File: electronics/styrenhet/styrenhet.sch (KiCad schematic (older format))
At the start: 50 parts, among them J1 12V Fan, J2 Battery_In, J3 Battery to MCU, J4 12V Fan, J5 IDE PATA Connector, J6 Motor1_In, J7 Motor2_In, J8 Motor3_In, J9 Motor4_In, U1 motor_driver, U2 motor_driver, U3 motor_driver, U4 motor_driver

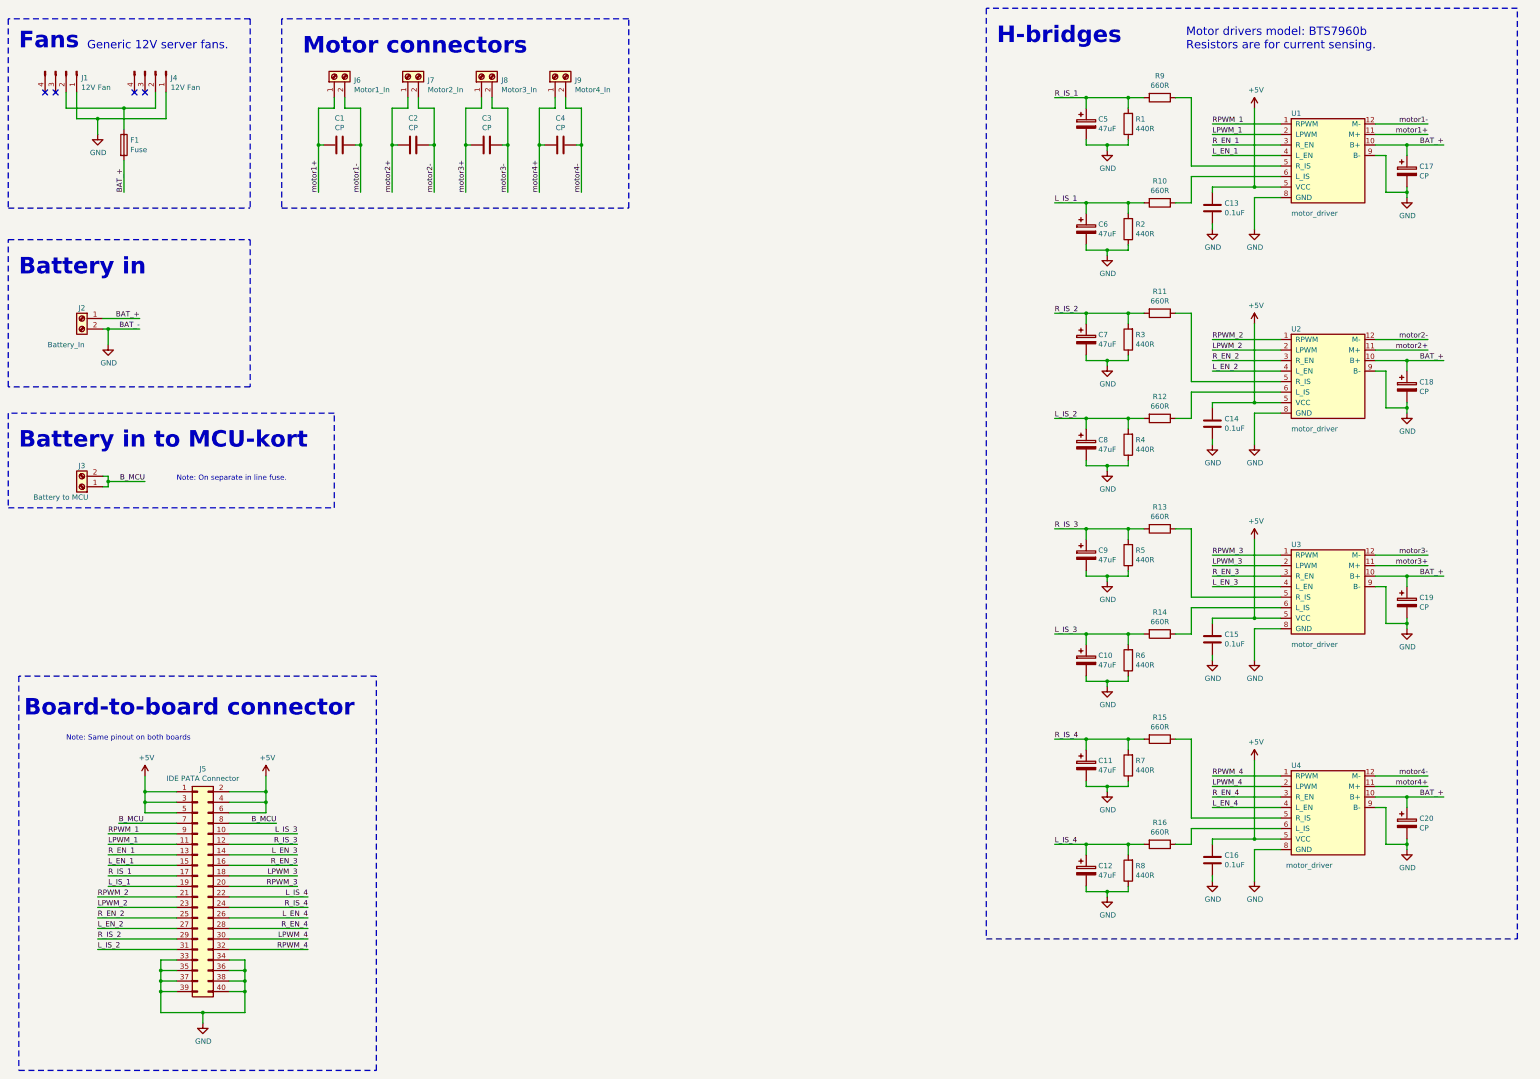
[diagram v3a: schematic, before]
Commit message: Placera h-bryggor.
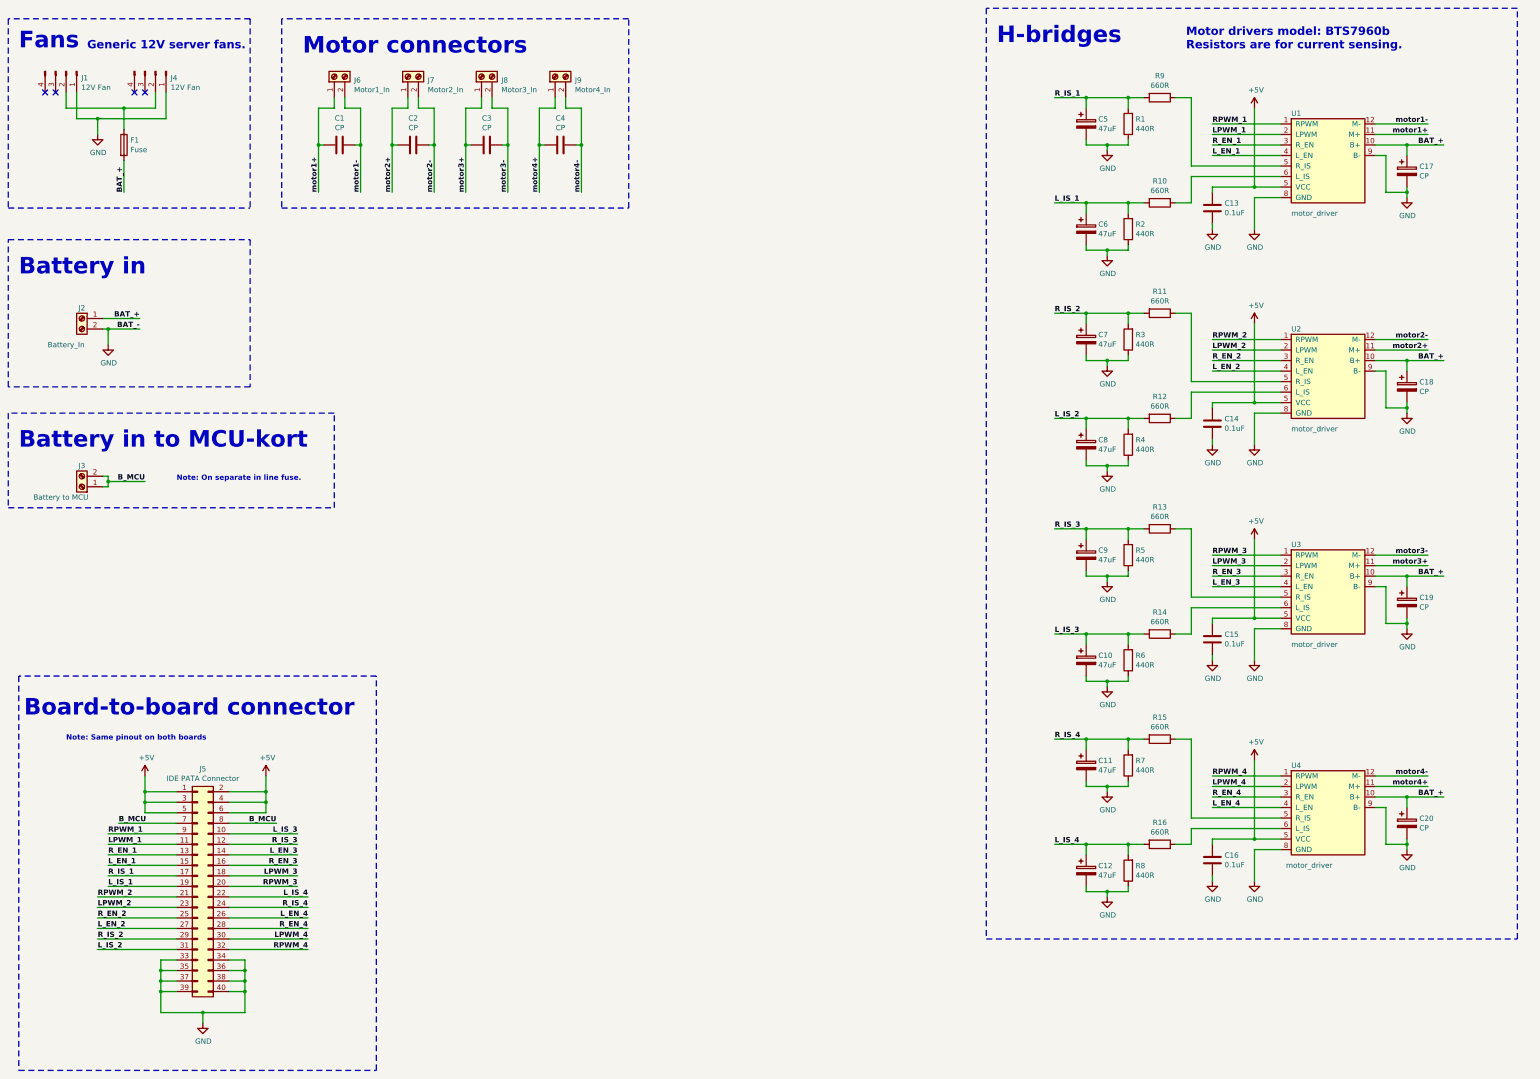
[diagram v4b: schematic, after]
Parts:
- U2, U3, U4: footprint styrenhet:motor-driver -> styrenhet-footprints:motor-driver
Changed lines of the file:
@@
 Wire Wire Line
 	12600 2750 12600 2800
-Text Label 12600 1800 0    50   ~ 0
+Text Label 12600 1800 0    50   ~ 6
 RPWM_1
 Wire Wire Line
 	12600 1800 13250 1800
-Text Label 12600 1900 0    50   ~ 0
+Text Label 12600 1900 0    50   ~ 6
 LPWM_1
 Wire Wire Line
 	12600 1900 13250 1900
-Text Label 12600 2000 0    50   ~ 0
+Text Label 12600 2000 0    50   ~ 6
 R_EN_1
-Text Label 12600 2100 0    50   ~ 0
+Text Label 12600 2100 0    50   ~ 6
 L_EN_1
-Text Label 11100 1550 0    50   ~ 0
+Text Label 11100 1550 0    50   ~ 6
 R_IS_1
 Wire Wire Line
@@
 F 0 "U2" H 13350 4650 50  0000 L CNN
 F 1 "motor_driver" H 13350 3700 50  0000 L CNN
-F 2 "styrenhet:motor-driver" H 13350 4150 50  0001 C CNN
+F 2 "styrenhet-footprints:motor-driver" H 13350 4150 50  0001 C CNN
 F 3 "" H 13350 4150 50  0001 C CNN
 	1    13700 4200
@@
 Wire Wire Line
 	12600 4800 12600 4850
-Text Label 12600 3850 0    50   ~ 0
+Text Label 12600 3850 0    50   ~ 6
 RPWM_2
 Wire Wire Line
 	12600 3850 13250 3850
-Text Label 12600 3950 0    50   ~ 0
+Text Label 12600 3950 0    50   ~ 6
 LPWM_2
 Wire Wire Line
 	12600 3950 13250 3950
-Text Label 12600 4050 0    50   ~ 0
+Text Label 12600 4050 0    50   ~ 6
 R_EN_2
-Text Label 12600 4150 0    50   ~ 0
+Text Label 12600 4150 0    50   ~ 6
 L_EN_2
-Text Label 11100 3600 0    50   ~ 0
+Text Label 11100 3600 0    50   ~ 6
 R_IS_2
-Text Label 11100 4600 0    50   ~ 0
+Text Label 11100 4600 0    50   ~ 6
 L_IS_2
 Wire Wire Line
@@
 Wire Wire Line
 	12600 6850 12600 6900
-Text Label 12600 5900 0    50   ~ 0
+Text Label 12600 5900 0    50   ~ 6
 RPWM_3
 Wire Wire Line
 	12600 5900 13250 5900
-Text Label 12600 6000 0    50   ~ 0
+Text Label 12600 6000 0    50   ~ 6
 LPWM_3
 Wire Wire Line
 	12600 6000 13250 6000
-Text Label 12600 6100 0    50   ~ 0
+Text Label 12600 6100 0    50   ~ 6
 R_EN_3
-Text Label 12600 6200 0    50   ~ 0
+Text Label 12600 6200 0    50   ~ 6
 L_EN_3
-Text Label 11100 5650 0    50   ~ 0
+Text Label 11100 5650 0    50   ~ 6
 R_IS_3
-Text Label 11100 6650 0    50   ~ 0
+Text Label 11100 6650 0    50   ~ 6
 L_IS_3
 Wire Wire Line
@@
 F 0 "U4" H 13350 8800 50  0000 L CNN
 F 1 "motor_driver" H 13300 7850 50  0000 L CNN
-F 2 "styrenhet:motor-driver" H 13350 8300 50  0001 C CNN
+F 2 "styrenhet-footprints:motor-driver" H 13350 8300 50  0001 C CNN
 F 3 "" H 13350 8300 50  0001 C CNN
 	1    13700 8350
@@
 Wire Wire Line
 	12600 8950 12600 9000
-Text Label 12600 8000 0    50   ~ 0
+Text Label 12600 8000 0    50   ~ 6
 RPWM_4
 Wire Wire Line
 	12600 8000 13250 8000
-Text Label 12600 8100 0    50   ~ 0
+Text Label 12600 8100 0    50   ~ 6
 LPWM_4
 Wire Wire Line
 	12600 8100 13250 8100
-Text Label 12600 8200 0    50   ~ 0
+Text Label 12600 8200 0    50   ~ 6
 R_EN_4
-Text Label 12600 8300 0    50   ~ 0
+Text Label 12600 8300 0    50   ~ 6
 L_EN_4
-Text Label 11100 7650 0    50   ~ 0
+Text Label 11100 7650 0    50   ~ 6
 R_IS_4
-Text Label 11100 8650 0    50   ~ 0
+Text Label 11100 8650 0    50   ~ 6
 L_IS_4
 Wire Wire Line
@@
 	0    1    1    0
 $EndComp
-Text Label 2250 2450 1    50   ~ 0
+Text Label 2250 2450 1    50   ~ 6
 BAT_+
 Wire Wire Line
@@
 Wire Wire Line
 	2600 10050 2600 10250
-Text Label 3900 9050 2    50   ~ 0
+Text Label 3900 9050 2    50   ~ 6
 RPWM_3
 Wire Wire Line
 	3900 9050 3250 9050
-Text Label 3900 8950 2    50   ~ 0
+Text Label 3900 8950 2    50   ~ 6
 LPWM_3
 Wire Wire Line
 	3900 8950 3250 8950
-Text Label 3900 8850 2    50   ~ 0
+Text Label 3900 8850 2    50   ~ 6
 R_EN_3
-Text Label 3900 8750 2    50   ~ 0
+Text Label 3900 8750 2    50   ~ 6
 L_EN_3
-Text Label 3900 8650 2    50   ~ 0
+Text Label 3900 8650 2    50   ~ 6
 R_IS_3
-Text Label 3900 8550 2    50   ~ 0
+Text Label 3900 8550 2    50   ~ 6
 L_IS_3
 Wire Wire Line
@@
 Wire Wire Line
 	3250 8850 3900 8850
-Text Label 2100 8550 0    50   ~ 0
+Text Label 2100 8550 0    50   ~ 6
 RPWM_1
 Wire Wire Line
 	2100 8550 2750 8550
-Text Label 2100 8650 0    50   ~ 0
+Text Label 2100 8650 0    50   ~ 6
 LPWM_1
 Wire Wire Line
 	2100 8650 2750 8650
-Text Label 2100 8750 0    50   ~ 0
+Text Label 2100 8750 0    50   ~ 6
 R_EN_1
-Text Label 2100 8850 0    50   ~ 0
+Text Label 2100 8850 0    50   ~ 6
 L_EN_1
-Text Label 2100 8950 0    50   ~ 0
+Text Label 2100 8950 0    50   ~ 6
 R_IS_1
-Text Label 2100 9050 0    50   ~ 0
+Text Label 2100 9050 0    50   ~ 6
 L_IS_1
 Wire Wire Line
@@
 Wire Wire Line
 	2750 8750 2100 8750
-Text Label 2000 9150 0    50   ~ 0
+Text Label 2000 9150 0    50   ~ 6
 RPWM_2
-Text Label 2000 9250 0    50   ~ 0
+Text Label 2000 9250 0    50   ~ 6
 LPWM_2
-Text Label 2000 9350 0    50   ~ 0
+Text Label 2000 9350 0    50   ~ 6
 R_EN_2
-Text Label 2000 9450 0    50   ~ 0
+Text Label 2000 9450 0    50   ~ 6
 L_EN_2
-Text Label 2000 9550 0    50   ~ 0
+Text Label 2000 9550 0    50   ~ 6
 R_IS_2
-Text Label 2000 9650 0    50   ~ 0
+Text Label 2000 9650 0    50   ~ 6
 L_IS_2
-Text Label 4000 9650 2    50   ~ 0
+Text Label 4000 9650 2    50   ~ 6
 RPWM_4
-Text Label 4000 9550 2    50   ~ 0
+Text Label 4000 9550 2    50   ~ 6
 LPWM_4
-Text Label 4000 9450 2    50   ~ 0
+Text Label 4000 9450 2    50   ~ 6
 R_EN_4
-Text Label 4000 9350 2    50   ~ 0
+Text Label 4000 9350 2    50   ~ 6
 L_EN_4
-Text Label 4000 9250 2    50   ~ 0
+Text Label 4000 9250 2    50   ~ 6
 R_IS_4
-Text Label 4000 9150 2    50   ~ 0
+Text Label 4000 9150 2    50   ~ 6
 L_IS_4
 Wire Wire Line
@@
 Wire Wire Line
 	3250 9150 4000 9150
-Text Notes 1700 7750 0    50   ~ 0
+Text Notes 1700 7750 0    50   ~ 6
 Note: Same pinout on both boards\n\n
 $Comp
@@
 Wire Wire Line
 	12400 8500 13250 8500
-Text Notes 12350 1100 0    79   ~ 0
+Text Notes 12350 1100 0    79   ~ 6
 Motor drivers model: BTS7960b\nResistors are for current sensing.\n
 Text Notes 1300 7950 0    157  ~ 31
@@
 Wire Notes Line
 	3450 800  1150 800
-Text Notes 1900 1100 0    79   ~ 0
+Text Notes 1900 1100 0    79   ~ 6
 Generic 12V server fans.\n
 $Comp
@@
 Wire Wire Line
 	2250 2150 2250 2450
-Text Label 14650 3950 2    50   ~ 0
+Text Label 14650 3950 2    50   ~ 6
 motor2+
-Text Label 14650 3850 2    50   ~ 0
+Text Label 14650 3850 2    50   ~ 6
 motor2-
 Wire Wire Line
@@
 Wire Wire Line
 	14150 3950 14650 3950
-Text Label 14650 6000 2    50   ~ 0
+Text Label 14650 6000 2    50   ~ 6
 motor3+
-Text Label 14650 5900 2    50   ~ 0
+Text Label 14650 5900 2    50   ~ 6
 motor3-
 Wire Wire Line
@@
 Wire Wire Line
 	14150 6000 14650 6000
-Text Label 14650 8100 2    50   ~ 0
+Text Label 14650 8100 2    50   ~ 6
 motor4+
-Text Label 14650 8000 2    50   ~ 0
+Text Label 14650 8000 2    50   ~ 6
 motor4-
 Wire Wire Line
@@
 F 0 "U3" H 13350 6700 50  0000 L CNN
 F 1 "motor_driver" H 13350 5750 50  0000 L CNN
-F 2 "styrenhet:motor-driver" H 13350 6200 50  0001 C CNN
+F 2 "styrenhet-footprints:motor-driver" H 13350 6200 50  0001 C CNN
 F 3 "" H 13350 6200 50  0001 C CNN
 	1    13700 6250
 	1    0    0    -1
 $EndComp
-Text Label 14800 2000 2    50   ~ 0
+Text Label 14800 2000 2    50   ~ 6
 BAT_+
 $Comp
@@
 	-1   0    0    -1
 $EndComp
-Text Label 2400 3650 2    50   ~ 0
+Text Label 2400 3650 2    50   ~ 6
 BAT_+
-Text Label 2400 3750 2    50   ~ 0
+Text Label 2400 3750 2    50   ~ 6
 BAT_-
 Wire Wire Line
@@
 Wire Wire Line
 	6200 2000 6200 2450
-Text Label 6600 2450 1    50   ~ 0
+Text Label 6600 2450 1    50   ~ 6
 motor4-
-Text Label 6200 2450 1    50   ~ 0
+Text Label 6200 2450 1    50   ~ 6
 motor4+
 Wire Wire Line
@@
 Wire Wire Line
 	5500 2000 5500 2450
-Text Label 5900 2450 1    50   ~ 0
+Text Label 5900 2450 1    50   ~ 6
 motor3-
-Text Label 5500 2450 1    50   ~ 0
+Text Label 5500 2450 1    50   ~ 6
 motor3+
 Wire Wire Line
@@
 Wire Wire Line
 	4800 2000 4800 2450
-Text Label 5200 2450 1    50   ~ 0
+Text Label 5200 2450 1    50   ~ 6
 motor2-
-Text Label 4800 2450 1    50   ~ 0
+Text Label 4800 2450 1    50   ~ 6
 motor2+
 Connection ~ 6600 2000
@@
 	0    -1   -1   0
 $EndComp
-Text Label 4500 2450 1    50   ~ 0
+Text Label 4500 2450 1    50   ~ 6
 motor1-
-Text Label 4100 2450 1    50   ~ 0
+Text Label 4100 2450 1    50   ~ 6
 motor1+
 $Comp
@@
 	0    -1   -1   0
 $EndComp
-Text Label 14650 1900 2    50   ~ 0
+Text Label 14650 1900 2    50   ~ 6
 motor1+
-Text Label 14650 1800 2    50   ~ 0
+Text Label 14650 1800 2    50   ~ 6
 motor1-
 Wire Wire Line
@@
 	14450 2450 14450 2500
 Connection ~ 14450 2450
-Text Label 14800 4050 2    50   ~ 0
+Text Label 14800 4050 2    50   ~ 6
 BAT_+
 $Comp
@@
 	14450 4500 14450 4550
 Connection ~ 14450 4500
-Text Label 14800 6100 2    50   ~ 0
+Text Label 14800 6100 2    50   ~ 6
 BAT_+
 $Comp
@@
 	14450 6550 14450 6600
 Connection ~ 14450 6550
-Text Label 14800 8200 2    50   ~ 0
+Text Label 14800 8200 2    50   ~ 6
 BAT_+
 $Comp
@@
 	-1   0    0    1
 $EndComp
-Text Label 2450 5200 2    50   ~ 0
+Text Label 2450 5200 2    50   ~ 6
 B_MCU
 Wire Notes Line
@@
 Wire Notes Line
 	4250 4550 1150 4550
-Text Notes 2750 5200 0    50   ~ 0
+Text Notes 2750 5200 0    50   ~ 6
 Note: On separate in line fuse.
-Text Label 3700 8450 2    50   ~ 0
+Text Label 3700 8450 2    50   ~ 6
 B_MCU
-Text Label 2200 8450 0    50   ~ 0
+Text Label 2200 8450 0    50   ~ 6
 B_MCU
 $Comp
@@
 	11100 1550 11400 1550
 Connection ~ 11400 1550
-Text Label 11100 2550 0    50   ~ 0
+Text Label 11100 2550 0    50   ~ 6
 L_IS_1
 $Comp
